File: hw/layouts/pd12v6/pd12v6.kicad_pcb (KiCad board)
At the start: 2 copper layers, 41 x 36 mm, 43 parts

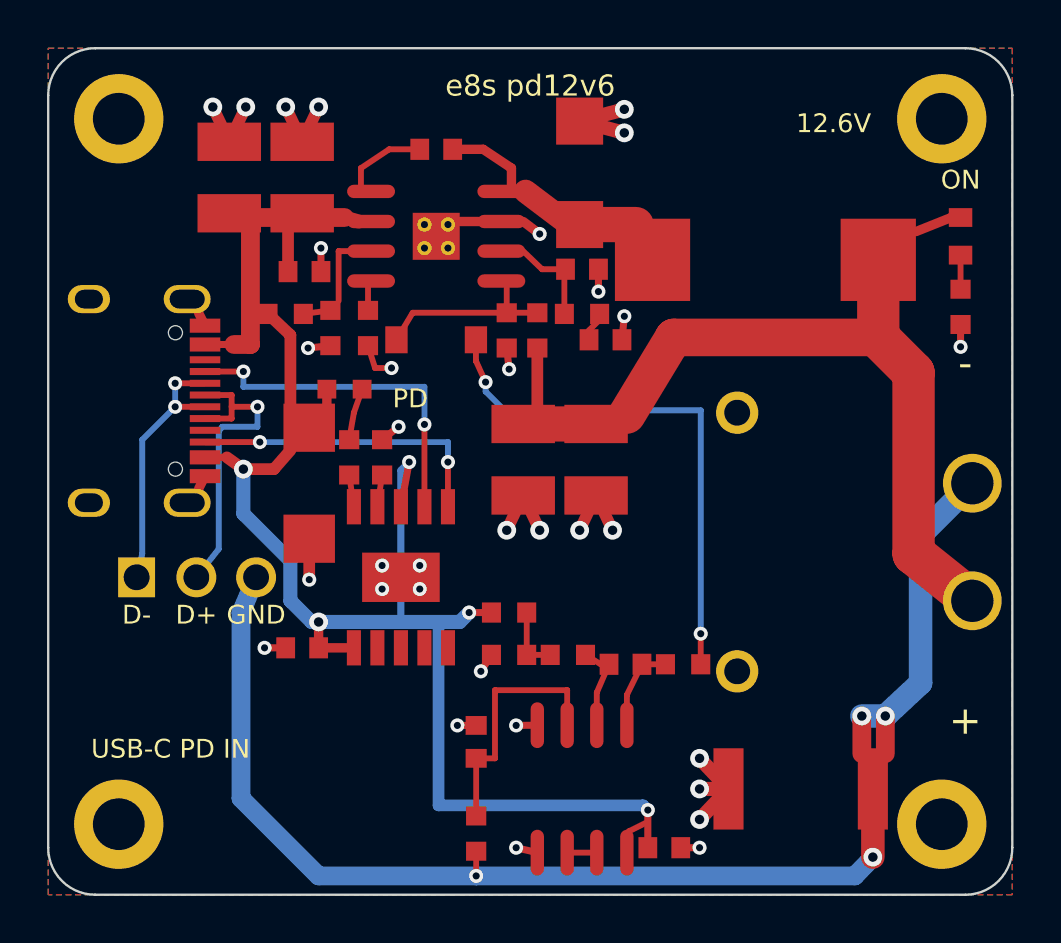
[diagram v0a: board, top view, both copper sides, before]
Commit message: pd12v6 rev A: 4-layer grid layout, Micro-Fit output, routed + hand-route copies
- Drop the LM358 current-limit block; single Molex Micro-Fit 3.0 2x2 output
  (1 +12.6 V, 2 GND, 3 D+, 4 D-), Sunlord MWSA0603S 10 uH inductor.
- 4-layer Sig/GND/PWR/Sig, 40 x 32 mm, inset silk frame, labelled pins.
- layout_pd12v6.py places on a grid; routes_pd12v6.py routes; DRC clean.
- --place-only writes layouts/pd12v6_manual/ (same placement, no tracks).
- review.sh renders both boards plus inner layers; docs updated.

Co-Authored-By: Claude Fable 5.1 <noreply@anthropic.com>
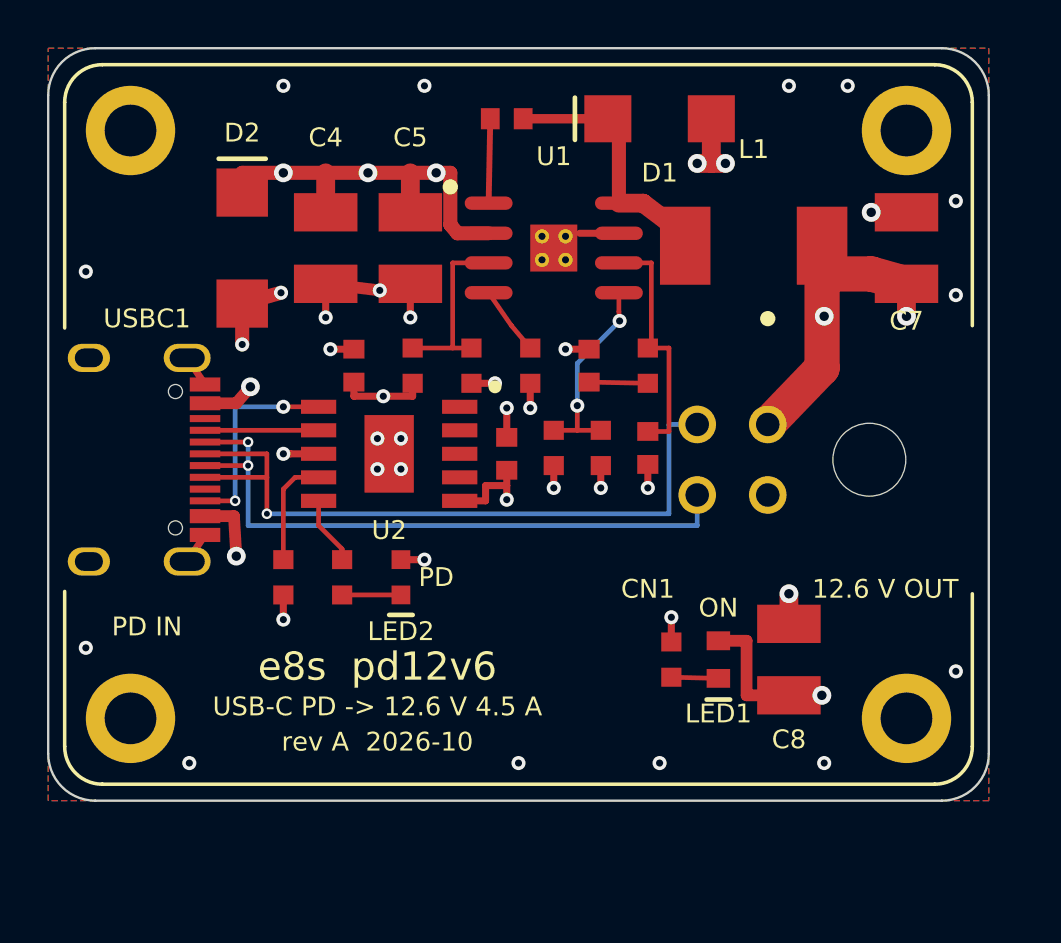
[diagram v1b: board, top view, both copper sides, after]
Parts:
- removed C10: , Chinocera_HGC1210R5476M250NSVK:C1210
- removed C11: , YAGEO_CC0603KRX7R9BB104:C0603
- removed C12: , SAMSUNG_CL10A105KB8NNNC:C0603
- removed D3: , MDD_SMBJ24A:SMB_L4.6-W3.6-LS5.3-RD
- removed J1: , HCTL_PZ254_1_03_Z_8_5:HDR-TH_03P-P2.54-V-M
- removed R10, R12: , UNI_ROYAL_0603WAF1001T5E:R0603
- removed R11: , UNI_ROYAL_0603WAF2403T5E:R0603
- removed R13: , PSA_FMF25FPJR020_LH:R2512
- removed R14: , UNI_ROYAL_0603WAF8203T5E:R0603
- removed R15: , UNI_ROYAL_0603WAF5602T5E:R0603
- removed U3: , WCH_CH224A:ESSOP-10_L4.9-W3.9-P1.0-LS6.0-TL-EP
- C7, C8: footprint YAGEO_CC0603KRX7R9BB104:C0603 -> Chinocera_HGC1210R5476M250NSVK:C1210
- C9: footprint Chinocera_HGC1210R5476M250NSVK:C1210 -> SAMSUNG_CL10A105KB8NNNC:C0603
- CN1: footprint AMASS_XT30PW_M30_G_Y:CONN-TH_XT30PW-M -> MOLEX_0430450400:CONN-TH_0430450400
- D2: footprint CJ_1N4148W:SOD-123_L2.8-W1.8-LS3.7-RD -> MDD_SMBJ24A:SMB_L4.6-W3.6-LS5.3-RD
- L1: footprint UNKNOWN_SL1040_100M:IND-SMD_L11.0-W10.2 -> Sunlord_MWSA0603S_100MT:IND-SMD_L7.1-W6.6
- R5: footprint UNI_ROYAL_0603WAF1003T5E:R0603 -> UNI_ROYAL_0603WAF4701T5E:R0603
- R7: footprint UNI_ROYAL_0603WAF4701T5E:R0603 -> UNI_ROYAL_0603WAF2403T5E:R0603
- R8: footprint UNI_ROYAL_0603WAF1002T5E:R0603 -> UNI_ROYAL_0603WAF8203T5E:R0603
- R9: footprint UNI_ROYAL_0603WAF2203T5E:R0603 -> UNI_ROYAL_0603WAF5602T5E:R0603
- U2: footprint onsemi_LM358DR2G:SOIC-8_L5.0-W4.0-P1.27-LS6.0-BL -> WCH_CH224A:ESSOP-10_L4.9-W3.9-P1.0-LS6.0-TL-EP
- moved C7 21.4 mm to (36.5, 8.50), turned to 90 degrees
- moved LED1 20.7 mm to (28.5, 26.0)
- moved R7 18.5 mm to (20.5, 13.5)
- moved U2 16.4 mm to (14.5, 17.2), turned to 90 degrees
- moved R9 10.6 mm to (18.0, 13.5), turned to -90 degrees
- moved R6 10.2 mm to (12.5, 22.5), turned to 90 degrees
- moved C8 9.60 mm to (31.5, 26.0), turned to 90 degrees
- moved D2 9.13 mm to (8.25, 8.50), turned to -90 degrees
- moved LED2 8.35 mm to (15.0, 22.5), turned to 90 degrees
- moved C5 8.26 mm to (15.4, 8.50), turned to -90 degrees
- moved C2 8.10 mm to (25.5, 17.0), turned to -90 degrees
- moved R1 6.61 mm to (10.0, 22.5), turned to -90 degrees
- moved R4 6.40 mm to (23.5, 17.0)
- moved CN1 6.27 mm to (29.1, 17.5), turned to 90 degrees
- moved R3 5.05 mm to (21.5, 17.0)
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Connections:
- C7 pad 1: I_OUT -> VOUT
- C7 pad 2: I_INT -> GND
- C8 pad 1: VBUS -> VOUT
- C9 pad 1: VOUT -> VBUS
- CN1 pad 1: OUT_RTN -> VOUT
- CN1 pad 2: VOUT -> GND
- CN1 pad 3: 3 -> USB_DP
- CN1 pad 4: 4 -> USB_DN
- D2 pad 1: FB -> VBUS
- D2 pad 2: I_INJ -> GND
- R5 pad 1: I_OUT -> LED_OUT_K
- R5 pad 2: I_INJ -> GND
- R6 pad 1: I_REF -> LED_PD_K
- R6 pad 2: I_INT -> PG_n
- R7 pad 1: LED_OUT_K -> RT
- R8 pad 1: LED_PD_K -> VBUS
- R8 pad 2: PG_n -> EN
- R9 pad 1: VBUS -> EN
- R9 pad 2: I_REF -> GND
- U2 pad 1: I_OUT -> VBUS
- U2 pad 2: I_INT -> CFG2_SCL
- U2 pad 3: I_SENSE -> CFG3_SDA
- U2 pad 4: GND -> DP
- U2 pad 5: GND -> DM
- U2 pad 6: P2INneg -> CC2
- U2 pad 7: P2INneg -> CC1
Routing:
- net OUT_RTN: track 56.0 -> 0.00 mm, vias 4 -> 0
- net VBUS: track 70.9 -> 32.3 mm, vias 5 -> 9
- net I_INJ: track 22.6 -> 0.00 mm, vias 2 -> 0
- net USB_DP: track 13.5 -> 29.9 mm
- net USB_DN: track 11.4 -> 27.6 mm
- net VOUT: track 36.4 -> 21.2 mm, vias 0 -> 4
- net I_SENSE: track 10.7 -> 0.00 mm
- net CC1: track 15.1 -> 4.83 mm, vias 2 -> 0
- net GND: track 39.7 -> 29.6 mm, vias 33 -> 35
- net COMP: track 3.56 -> 10.5 mm
- net CC2: track 13.1 -> 8.83 mm
- net EN: track 3.73 -> 7.65 mm
- net I_INT: track 3.81 -> 0.00 mm
- net I_OUT: track 3.74 -> 0.00 mm
- net CFG1: track 1.36 -> 4.71 mm
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- added copper zone on In1.Cu, net GND
- added copper zone on In2.Cu, net VBUS
- added copper zone on In2.Cu, net VOUT
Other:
- board size 41 x 36 mm -> 40 x 32 mm
- copper layers 2 -> 4
- board text added: "12.6 V OUT"
- board text added: "Micro-Fit 3.0: 1 +12.6V 2 GND 3 D+ 4 D-"
- board text added: "PD IN"
- board text added: "USB-C PD -> 12.6 V 4.5 A"
- board text added: "USB-C PD 65/100 W in. Output NOT current limited."
- board text added: "e8s pd12v6 rev A 2026-10"
- board text added: "rev A 2026-10"
- board text removed: "12.6V"
- board text removed: "GND"
- board text removed: "USB-C PD IN"
- board text removed: "e8s pd12v6 USB-C PD -> 12.6 V / 4.5 A"

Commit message: pd12v6: correct USB-C 3D model position, U2 pin-1 dot, 5 A label
- EasyEDA's TYPE-C-31-M-12 model sits 2.31 mm behind its own footprint
  (pins behind the pads, mouth inside the edge). KiCad's footprint for the
  same part confirms our copper; KiCad has no 3D model for it, so offset
  the EasyEDA model instead. Mouth now overhangs the edge by 0.9 mm.
- U2 pin-1 dot was by pin 5; moved to pin 1 (bottom-right).
- Title silk said 4.5 A (old current-limited design); now 5 A.

Co-Authored-By: Claude Opus 5.5 <noreply@anthropic.com>
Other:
- board text added: "USB-C PD -> 12.6 V 5 A"
- board text removed: "USB-C PD -> 12.6 V 4.5 A"
